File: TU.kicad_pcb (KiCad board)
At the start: 4 copper layers, 129 parts, among them IC1 CC1190, J1 Conn_01x06_Male, J2 Conn_01x17_Male, J3 Conn_Coaxial, J4 Debugger connector, J5 ARM_JTAG_SWD_10, J7 Conn_Coaxial, U1 ADP150AUJZ-3.3-R7, U2 SN65HVD233, U3 CC1200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

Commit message: More routing changes
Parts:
- removed G***: logo, KTHFS:logo
- removed J7: Conn_Coaxial, Connector_Coaxial:SMA_Amphenol_132134-10_Vertical
- added J6: Conn_01x05_Male, TU-HW RF LIB:Wurth_SMA_60312002114503, F.Cu at (92.7, 36.8)
- added R18: 0, Resistor_SMD:R_0603_1608Metric, F.Cu at (75.2, 46.5)
- added R19: 0, Resistor_SMD:R_0603_1608Metric, F.Cu at (102.7, 104.9)
- added R20: 0, Resistor_SMD:R_0603_1608Metric, F.Cu at (102.9, 107.9)
- J3: value Conn_Coaxial -> Conn_01x05_Male; footprint Connector_Coaxial:SMA_Amphenol_132134-10_Vertical -> TU-HW RF LIB:Wurth_SMA_60312002114503
- moved R12 38.6 mm to (89.5, 86.1), turned to 90 degrees
- moved J4 38.6 mm to (110.8, 98.7), turned to 0 degrees
- moved R11 38.2 mm to (91.0, 86.1), turned to 90 degrees
- moved R9 37.8 mm to (92.6, 86.1), turned to 90 degrees
- moved TP2 20.8 mm to (136.3, 100.4)
- moved J3 20.7 mm to (101.9, 36.8)
- moved C31 18.1 mm to (119.8, 93.0)
- moved C32 17.7 mm to (119.6, 95.5)
- moved C61 17.7 mm to (119.6, 97.0)
- moved J2 13.7 mm to (75.7, 51.0)
- moved Y1 4.07 mm to (99.7, 84.9), turned to 180 degrees
- moved C29 3.51 mm to (109.9, 86.2)
- moved C58 3.40 mm to (95.3, 86.1), turned to 90 degrees
- moved C59 3.38 mm to (96.9, 86.1), turned to 90 degrees
- moved C18 3.32 mm to (100.2, 54.0)
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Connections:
- net /transceiver/~RESET renamed /~RESET
- IC1 pad 6: /CC1190/HGM -> Net-(IC1-Pad6)
- IC1 pad 7: /CC1190/LNA_EN -> Net-(IC1-Pad7)
- IC1 pad 8: /CC1190/PA_EN -> Net-(IC1-Pad8)
- J2 pad 10: /MCU/MISO -> /MISO_RF2
- J2 pad 11: /MCU/MOSI -> /MOSI_RF2
- J2 pad 12: /transceiver/SCLK -> /SCLK_RF2
- J2 pad 13: /MCU/~CS_2 -> /~CS_RF2
- J2 pad 15: (no net) -> /DIO5
- J2 pad 17: (no net) -> GND
- J2 pad 3: (no net) -> /DIO3
- J2 pad 4: (no net) -> /DIO4
- J2 pad 5: +5V -> Net-(J2-Pad5)
- J2 pad 6: (no net) -> /DIO0
- J2 pad 7: (no net) -> /DIO1
- J2 pad 8: (no net) -> /DIO2
- J4 pad 10: /MCU/MISO -> /MISO
- J4 pad 3: (no net) -> /GPIO2
- J4 pad 4: (no net) -> /GPIO0
- J4 pad 5: /MCU/~CS_2 -> /~CS_1
- J4 pad 6: /transceiver/SCLK -> /SCLK
- J4 pad 8: /MCU/MOSI -> /MOSI
- R11 pad 2: /CC1190/LNA_EN -> Net-(IC1-Pad7)
- R12 pad 2: /CC1190/PA_EN -> Net-(IC1-Pad6)
- R9 pad 2: /CC1190/HGM -> Net-(IC1-Pad8)
- U3 pad 10: /transceiver/GPIO0 -> /GPIO0
- U3 pad 11: /transceiver/~CS -> /~CS_1
- U3 pad 4: /transceiver/GPIO2 -> /GPIO2
- U3 pad 7: /MCU/MOSI -> /MOSI
- U3 pad 8: /transceiver/SCLK -> /SCLK
- U3 pad 9: /MCU/MISO -> /MISO
- U4 pad 25: /transceiver/~CS -> (no net)
- U4 pad 26: /MCU/~CS_2 -> /~CS_RF2
- U4 pad 3: (no net) -> /CC1190/HGM
- U4 pad 30: /transceiver/SCLK -> /SCLK_RF2
- U4 pad 31: /MCU/MISO -> /MISO_RF2
- U4 pad 32: /MCU/MOSI -> /MOSI_RF2
- U4 pad 33: (no net) -> /DIO5
- U4 pad 34: (no net) -> /DIO3
- U4 pad 35: (no net) -> /DIO4
- U4 pad 36: (no net) -> /DIO0
- U4 pad 37: (no net) -> /DIO1
- U4 pad 38: (no net) -> /DIO2
- U4 pad 4: (no net) -> /CC1190/LNA_EN
- U4 pad 5: (no net) -> /CC1190/PA_EN
- U4 pad 78: (no net) -> /SCLK
- U4 pad 79: (no net) -> /MISO
- U4 pad 80: (no net) -> /MOSI
- U4 pad 87: (no net) -> Net-(R20-Pad2)
- U4 pad 89: (no net) -> /GPIO0
- U4 pad 90: /CC1190/HGM -> /GPIO2
- U4 pad 91: /CC1190/LNA_EN -> /transceiver/GPIO3
- U4 pad 92: /CC1190/PA_EN -> (no net)
- U4 pad 93: /transceiver/GPIO3 -> Net-(R19-Pad2)
- U4 pad 95: /transceiver/GPIO2 -> (no net)
- U4 pad 96: /transceiver/GPIO0 -> (no net)
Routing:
- net +5V: track 27.5 -> 151.5 mm
- net /DIO3: track 0.00 -> 74.7 mm
- net /DIO0: track 0.00 -> 73.4 mm
- net /DIO4: track 0.00 -> 73.2 mm
- net /DIO2: track 0.00 -> 72.5 mm
- net /DIO1: track 0.00 -> 72.4 mm
- net /MCU/~CS_2: track 51.1 -> 0.00 mm
- net /DIO5: track 0.00 -> 49.2 mm
- net /SCLK: track 0.00 -> 49.1 mm, vias 0 -> 1
- net /transceiver/SCLK: track 48.0 -> 0.00 mm
- net /MISO: track 0.00 -> 47.5 mm, vias 0 -> 2
- net /MCU/MISO: track 46.0 -> 0.00 mm
- net /MOSI: track 0.00 -> 43.5 mm, vias 0 -> 1
- net /~CS_1: track 0.00 -> 39.7 mm, vias 0 -> 1
- net /MOSI_RF2: track 0.00 -> 39.5 mm
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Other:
- board text removed: "RF section"

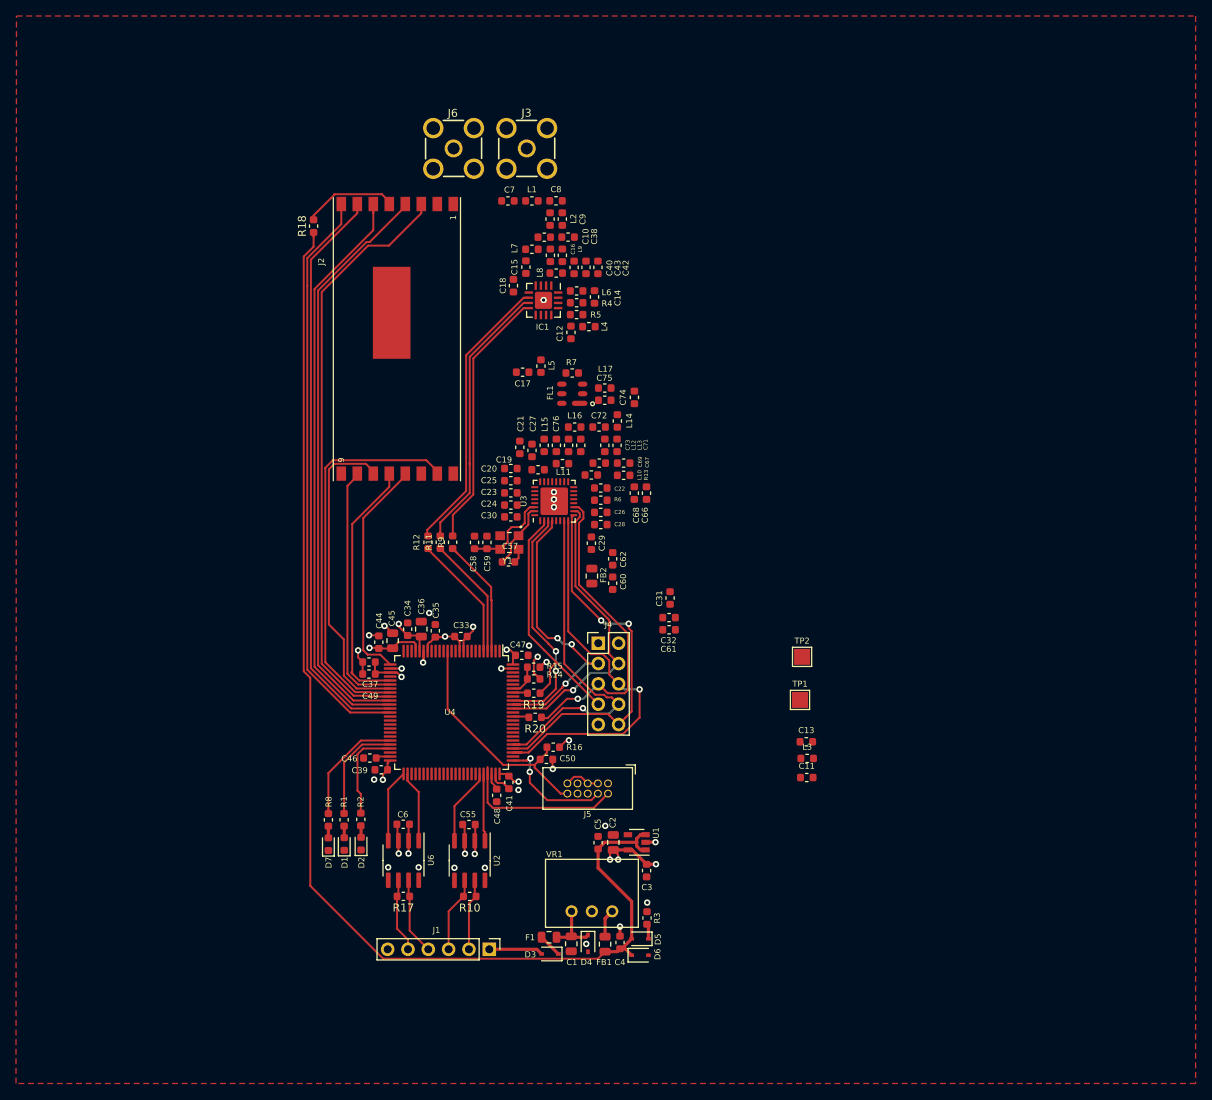
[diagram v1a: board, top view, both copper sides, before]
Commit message: Added edge cuts and silk screen comments
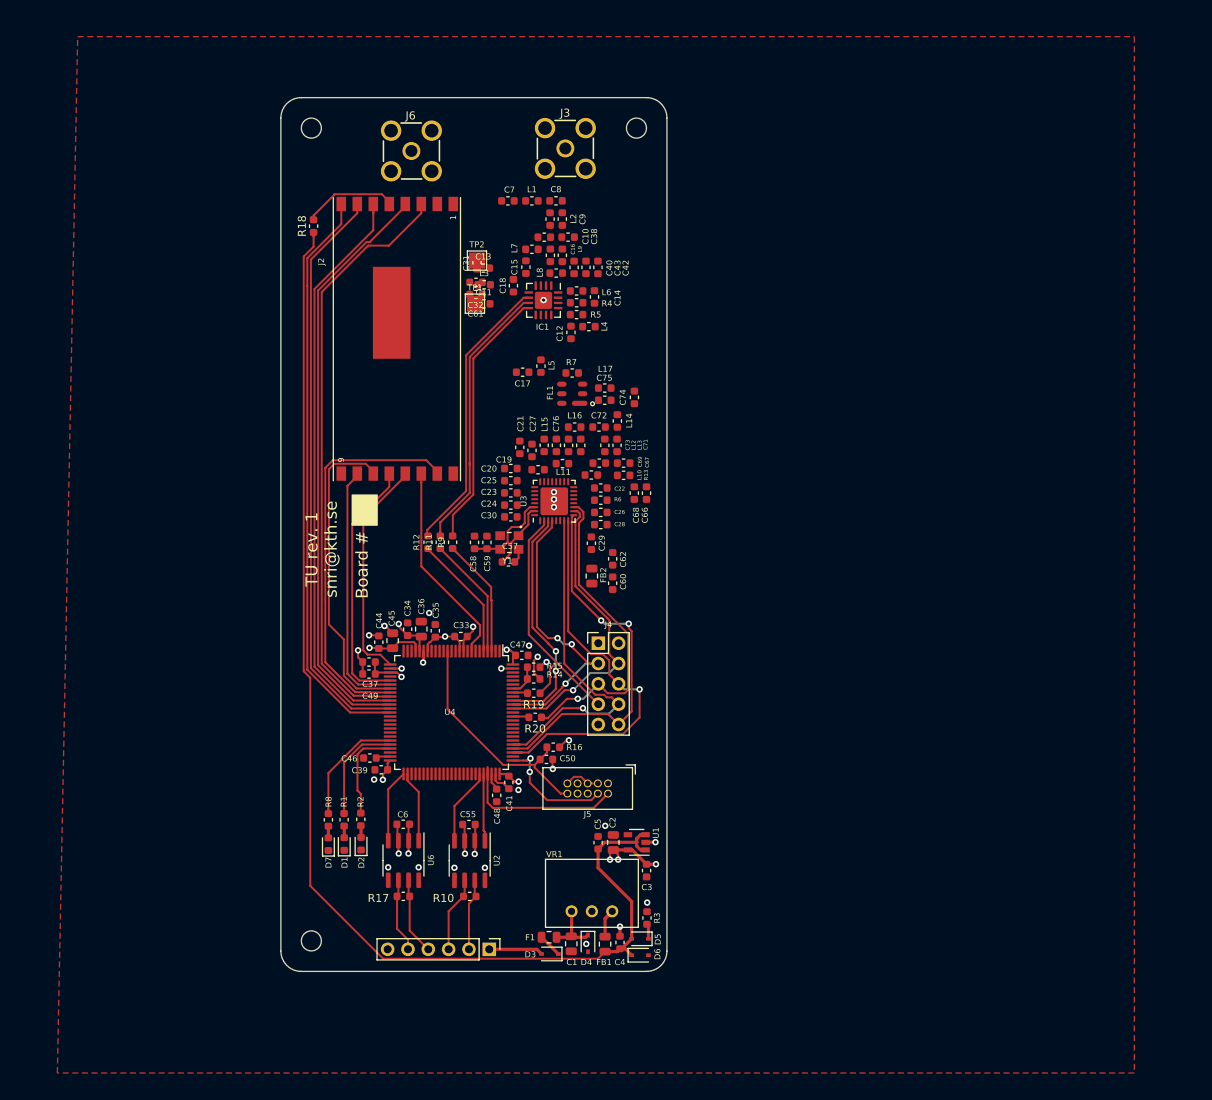
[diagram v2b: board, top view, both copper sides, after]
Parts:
- added REF**: MountingHole_2.5mm, MountingHole:MountingHole_2.5mm, F.Cu at (115.6, 34.3)
- added REF**: MountingHole_2.5mm, MountingHole:MountingHole_2.5mm, F.Cu at (74.9, 34.3)
- added REF**: MountingHole_2.5mm, MountingHole:MountingHole_2.5mm, F.Cu at (74.9, 135.9)
- moved C13 71.7 mm to (96.4, 51.8)
- moved C11 71.7 mm to (96.5, 56.3)
- moved L3 71.7 mm to (96.5, 53.9)
- moved TP1 64.1 mm to (95.4, 56.2)
- moved TP2 64.1 mm to (95.6, 50.9)
- moved C32 48.4 mm to (95.5, 53.6)
- moved C61 48.4 mm to (95.5, 55.1)
- moved C31 48.4 mm to (95.6, 51.1)
- moved J6 5.28 mm to (87.4, 37.1)
- moved J3 4.83 mm to (106.7, 36.8)
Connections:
- J2 pad 14: (no net) -> /RESET_RF2
- U4 pad 8: (no net) -> /RESET_RF2
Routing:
- net /RESET_RF2: track 0.00 -> 25.7 mm
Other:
- board outline added: 48.3 x 109.2 mm
- board text added: "+24V"
- board text added: "+3.3V"
- board text added: "Board #"
- board text added: "CAN1_H"
- board text added: "CAN1_L"
- board text added: "CAN2_H"
- board text added: "CAN2_L"
- board text added: "GND"
- board text added: "GPIO0"
- board text added: "GPIO2"
- board text added: "MISO"
- board text added: "MOSI"
- board text added: "SCLK"
- board text added: "TU rev. 1 snri@kth.se"
- board text added: "~CS_2"
- board text added: "~RESET"

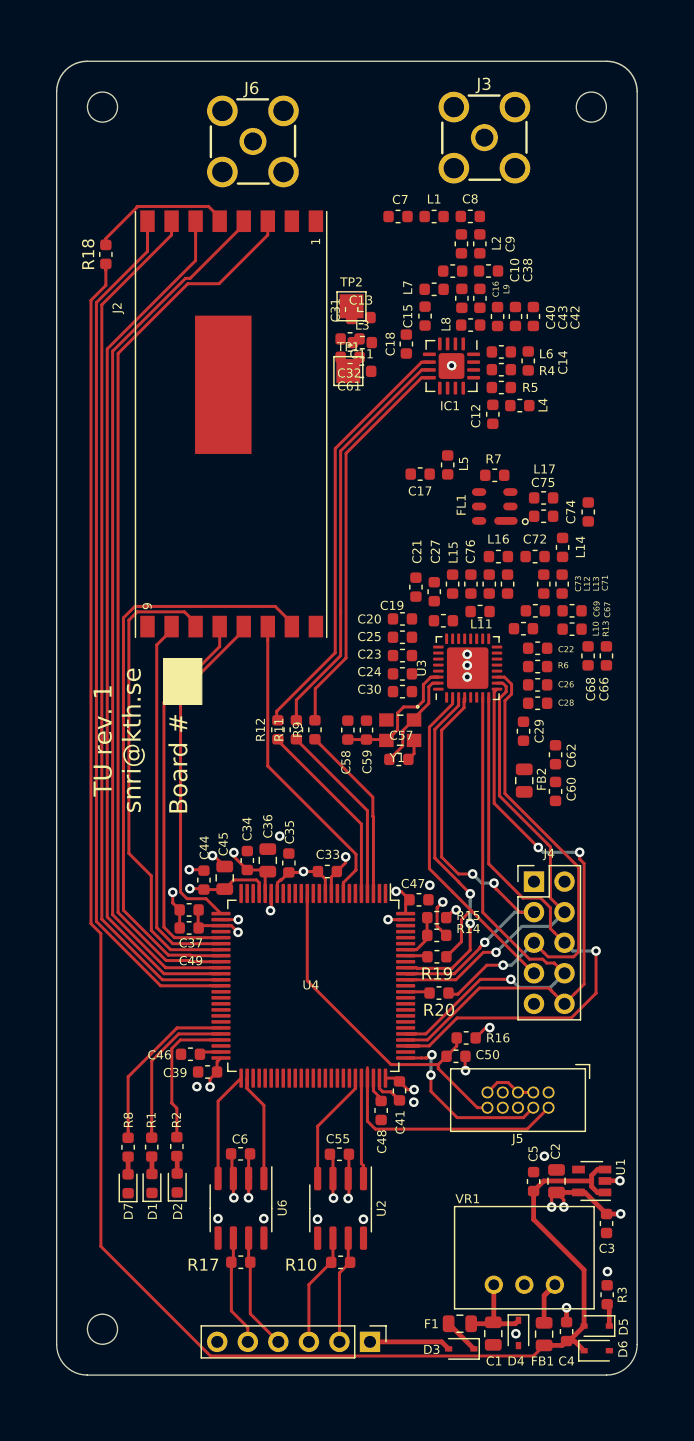
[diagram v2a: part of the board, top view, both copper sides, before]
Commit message: Added mounting holes and terminal block
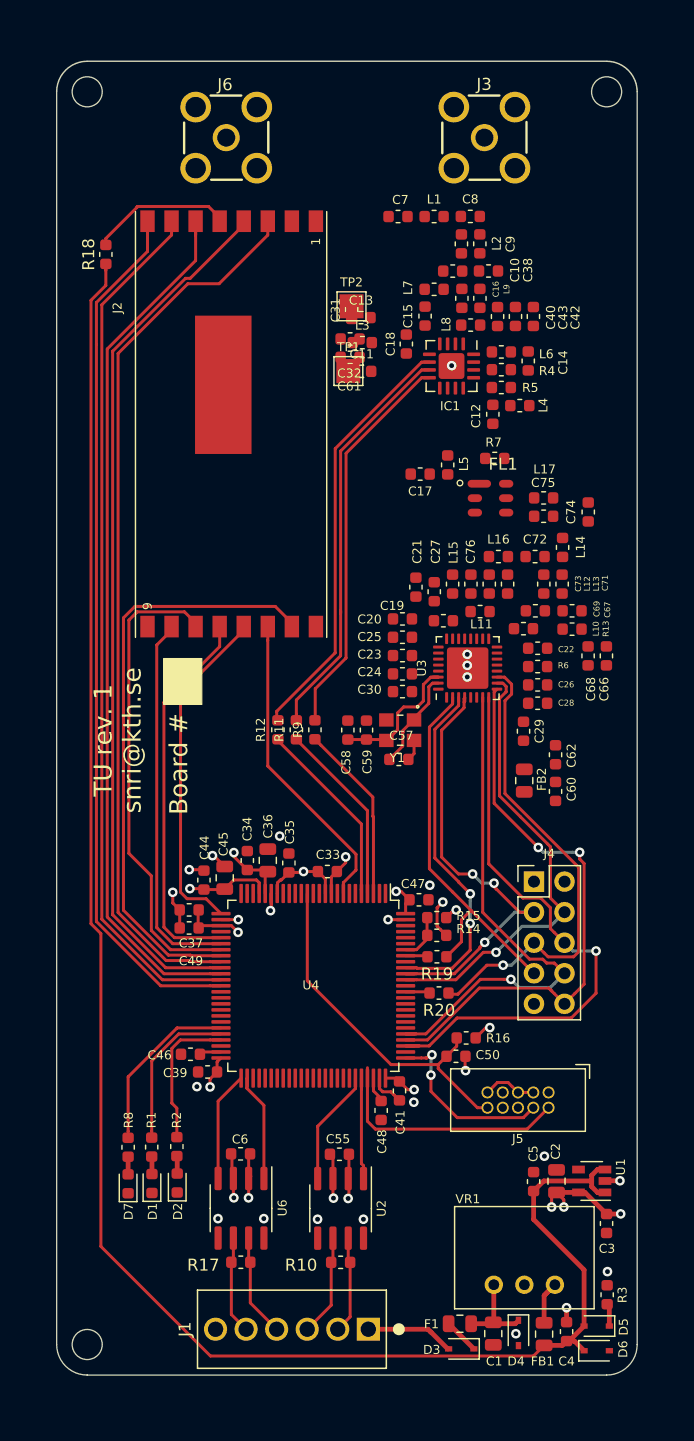
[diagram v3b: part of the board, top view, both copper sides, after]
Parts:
- removed REF** (x3): MountingHole_2.5mm, MountingHole:MountingHole_2.5mm
- added H1: MountingHole, MountingHole:MountingHole_2.5mm, F.Cu at (73.7, 33.0)
- added H2: MountingHole, MountingHole:MountingHole_2.5mm, F.Cu at (116.8, 33.0)
- added H3: MountingHole, MountingHole:MountingHole_2.5mm, F.Cu at (73.7, 137.2)
- J1: footprint Connector_PinHeader_2.54mm:PinHeader_1x06_P2.54mm_Vertical -> TU-HW RF LIB:TE_282834-6
- moved J1 6.58 mm to (90.7, 135.9), turned to 180 degrees
- moved J6 2.25 mm to (85.2, 36.8)
- moved R7 1.40 mm to (107.5, 63.5)
- moved FL1 0.77 mm to (107.2, 66.8), turned to 0 degrees
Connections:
- C75 pad 1: /CC1190/CC1190_RFIO -> /CC1190/RFIO
- FL1 pad 2: (no net) -> /CC1190/RFIO
- FL1 pad 5: (no net) -> Net-(C17-Pad1)
- L17 pad 2: /CC1190/CC1190_RFIO -> /CC1190/RFIO
- R7 pad 1: /CC1190/CC1190_RFIO -> /CC1190/RFIO
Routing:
- net /CAN_transceiver/CANL_2: track 9.27 -> 8.16 mm
- net /CAN_transceiver/CANH_2: track 9.65 -> 8.54 mm
- net /CAN_transceiver/CANH_1: track 9.05 -> 8.06 mm
- net /CAN_transceiver/CANL_1: track 9.45 -> 8.46 mm
- net /battery_in: track 6.78 -> 7.35 mm

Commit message: Small tweaks
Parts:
- moved J6 5.61 mm to (90.8, 37.3)
- moved C32 5.31 mm to (95.5, 48.3)
- moved J3 4.95 mm to (101.7, 36.9)
- moved J2 1.84 mm to (73.8, 51.0)
- moved R18 1.84 mm to (73.4, 46.5)
- moved TP1 1.84 mm to (93.5, 56.2)
- moved C29 0.59 mm to (110.5, 86.4)
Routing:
- net /DIO4: track 73.2 -> 75.3 mm
- net /DIO1: track 72.4 -> 74.4 mm
- net /DIO0: track 73.4 -> 75.4 mm
- net /RESET_RF2: track 25.7 -> 27.6 mm
- net /DIO3: track 74.7 -> 76.5 mm
- net /DIO2: track 72.5 -> 74.4 mm
- net /MOSI_RF2: track 39.5 -> 40.8 mm
- net /DIO5: track 49.2 -> 50.2 mm
- net +5V: track 151.5 -> 152.3 mm
- net /~CS_RF2: track 28.4 -> 27.6 mm
